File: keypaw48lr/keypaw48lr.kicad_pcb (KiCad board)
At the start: 2 copper layers, 139 x 102 mm, 103 parts, among them J1 Conn_01x02, J2 Conn_01x02, J3 Conn_01x02, J4 Conn_01x02, J5 Conn_01x02, J6 JD9613_OLED_FPC_Conn_01x10, J7 JD9613_OLED_FPC_Conn_01x10, SW1 SW_SPDT, SW2 RotaryEncoder, U1 nice_nano, U2 PAW3395, U3 TLV70019_SOT23-5, U4 TPS22917DBV

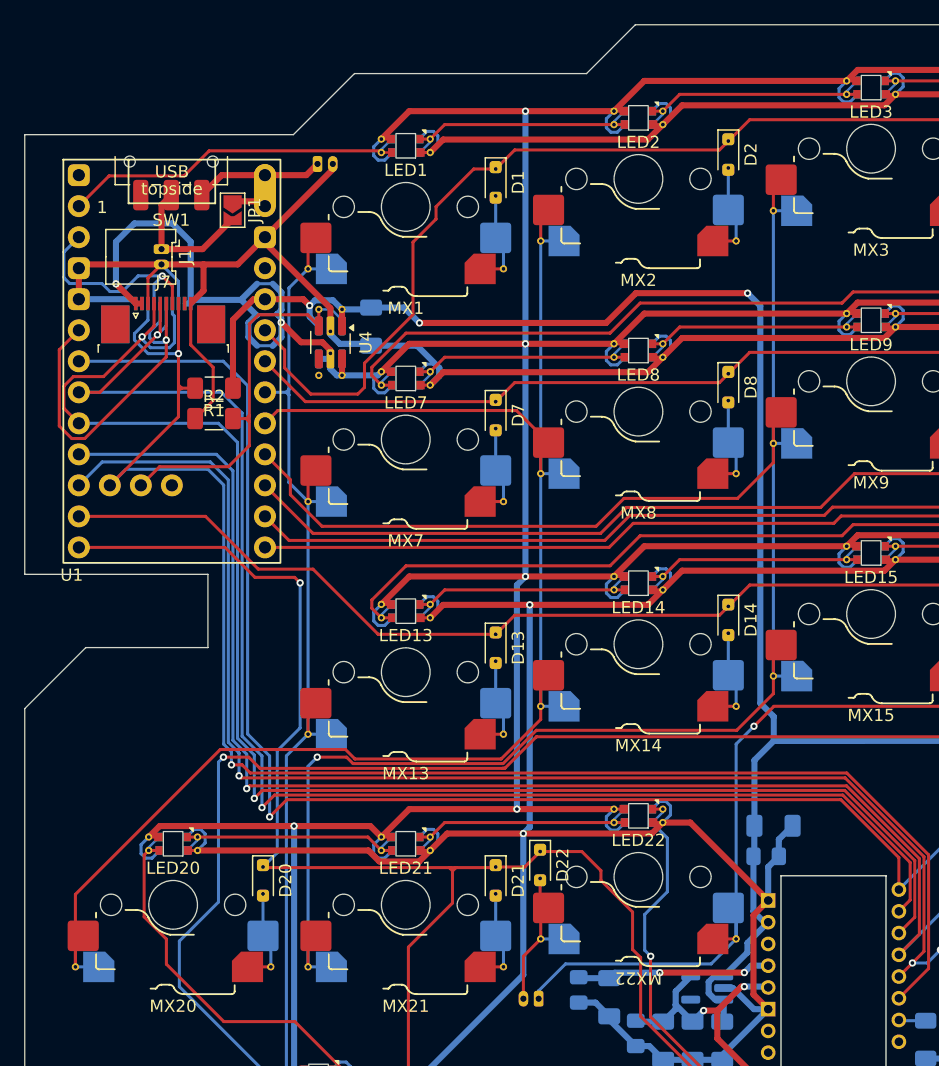
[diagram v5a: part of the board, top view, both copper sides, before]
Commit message: fix: should be able to solder nice!nano on both sides
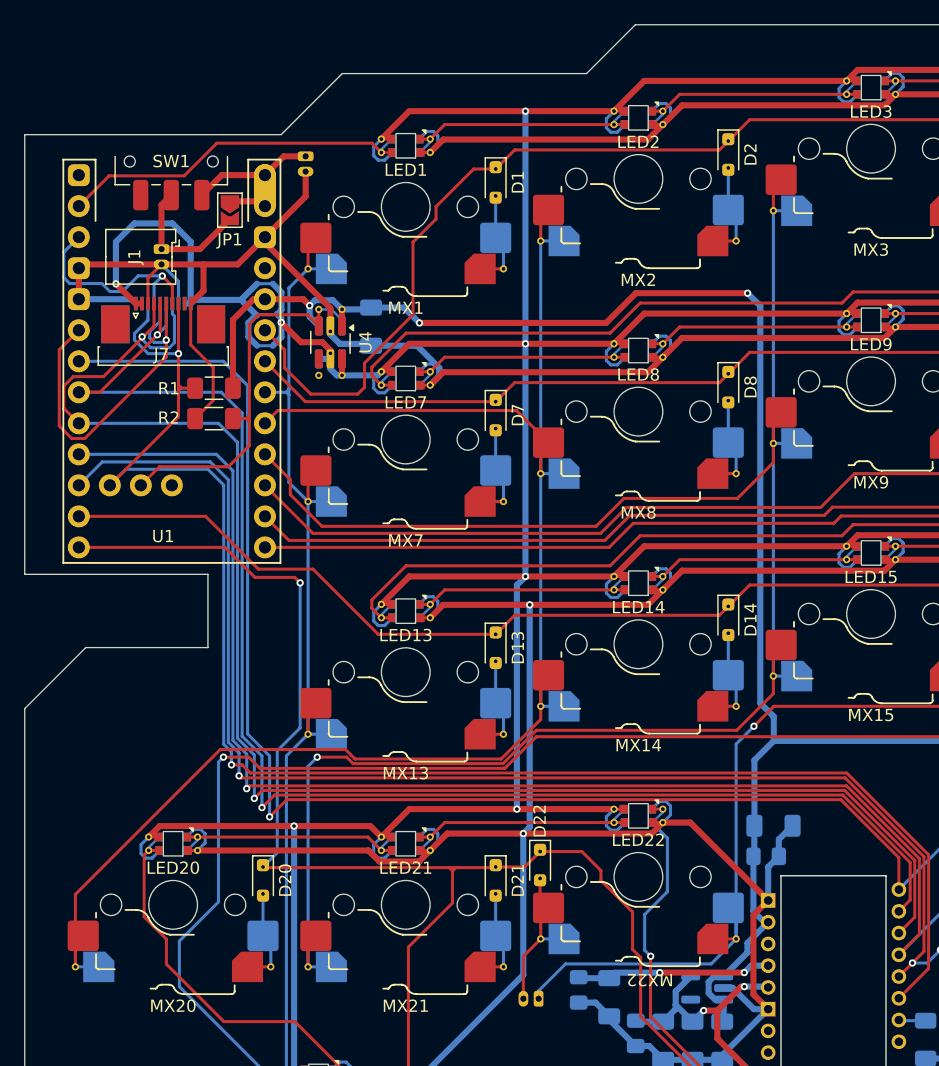
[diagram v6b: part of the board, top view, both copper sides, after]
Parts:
- U1: footprint PCM_marbastlib-xp-promicroish:nice_nano_AH_USBup -> MX_SW_HS_REV:nice_nano_AH_USBup_REV
- moved J2 1.16 mm to (68.0, 57.8), turned to -90 degrees
- moved JP1 0.22 mm to (61.8, 62.2)
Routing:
- net +3.3V: track 191.2 -> 184.0 mm
- net GND: track 761.0 -> 759.5 mm
- net LED: track 29.0 -> 29.5 mm
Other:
- outline, holes or cut-outs redrawn

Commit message: feat: add some more led lights
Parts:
- added LED25: WS2812B, WS2812B_2020_V6:LED_WS2812B-2020_backmount_rev, F.Cu at (56.0, 133.0)
- added LED26: WS2812B, WS2812B_2020_V6:LED_WS2812B-2020_backmount_rev, F.Cu at (85.0, 137.0)
- added LED27: WS2812B, WS2812B_2020_V6:LED_WS2812B-2020_backmount_rev, F.Cu at (119.8, 109.5)
- added LED28: WS2812B, WS2812B_2020_V6:LED_WS2812B-2020_backmount_rev, F.Cu at (132.4, 120.9)
- added LED29: WS2812B, WS2812B_2020_V6:LED_WS2812B-2020_backmount_rev, F.Cu at (152.0, 116.4)
- added LED30: WS2812B, WS2812B_2020_V6:LED_WS2812B-2020_backmount_rev, F.Cu at (171.8, 118.5)
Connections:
- LED19 pad 3: Net-(LED18-DOUT) -> Net-(LED19-DIN)
- LED20 pad 3: Net-(LED19-DOUT) -> Net-(LED20-DIN)
- LED24 pad 1: unconnected-(LED24-DOUT-Pad1) -> Net-(LED24-DOUT)
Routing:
- net GND: track 759.5 -> 896.7 mm
- net V_peri: track 639.4 -> 776.5 mm
- net Net-(LED24-DOUT): track 0.00 -> 76.6 mm
- net Net-(LED20-DIN): track 0.00 -> 52.8 mm
- net Net-(LED29-DOUT): track 0.00 -> 21.8 mm
- net Net-(LED28-DOUT): track 0.00 -> 21.6 mm
- net Net-(LED27-DOUT): track 0.00 -> 20.7 mm
- net Net-(LED19-DOUT): track 32.9 -> 18.6 mm
- net Net-(LED19-DIN): track 0.00 -> 14.2 mm
- net ROW3: track 194.6 -> 200.6 mm
- net Net-(LED18-DOUT): track 164.3 -> 159.5 mm, vias 3 -> 2
- net Net-(D24-A): track 21.7 -> 18.1 mm

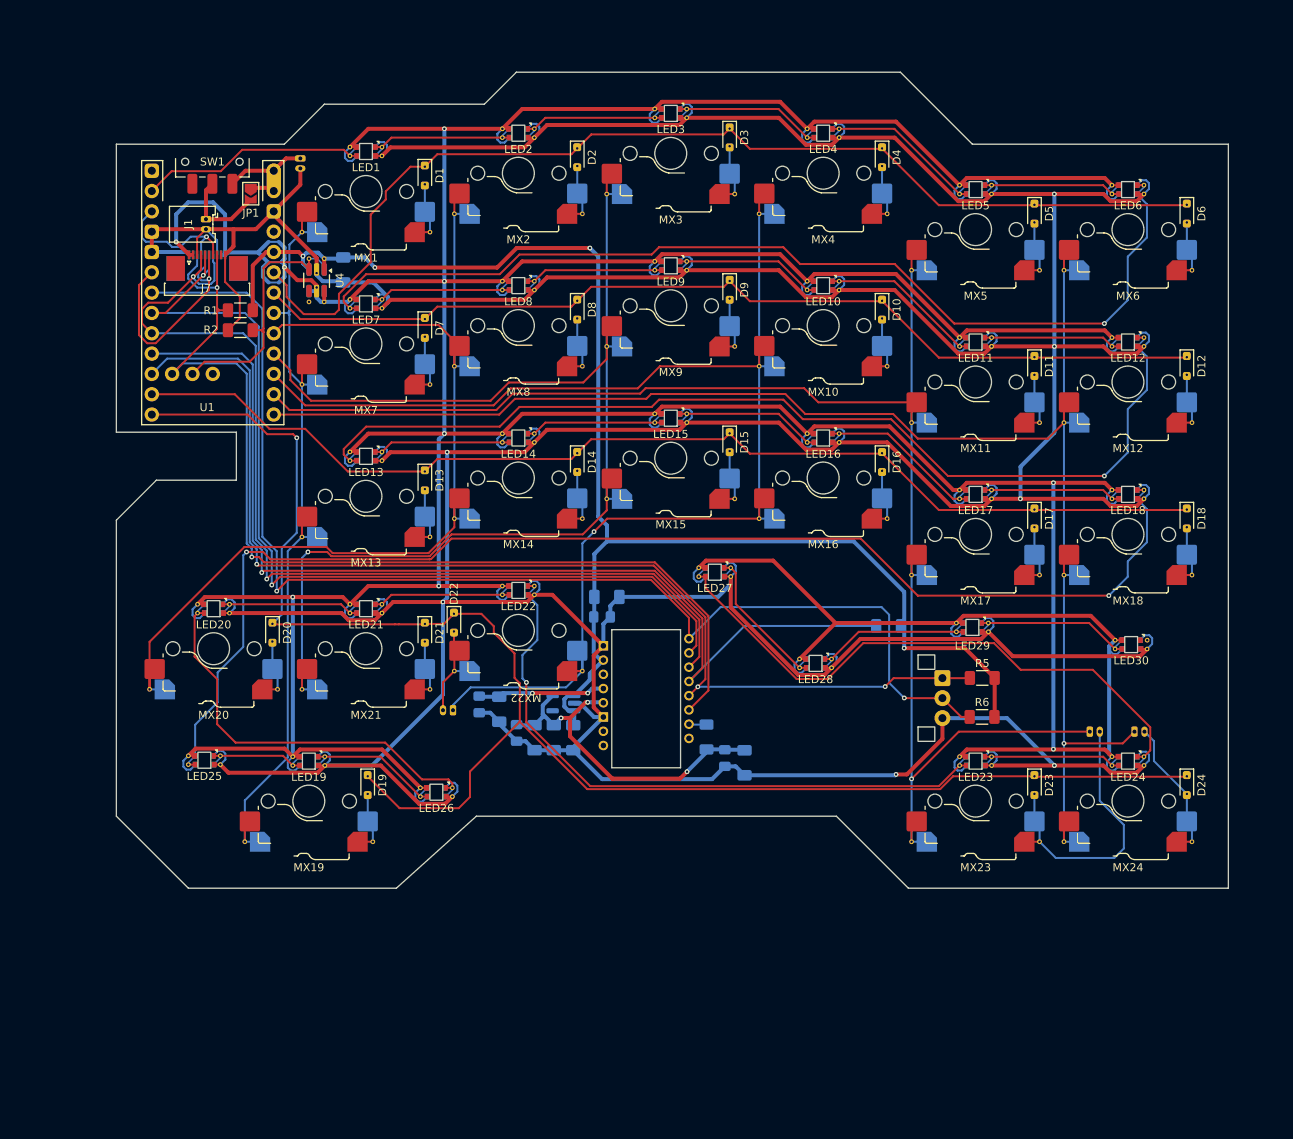
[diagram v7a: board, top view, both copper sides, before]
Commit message: feat: replace encoder with a touch bar
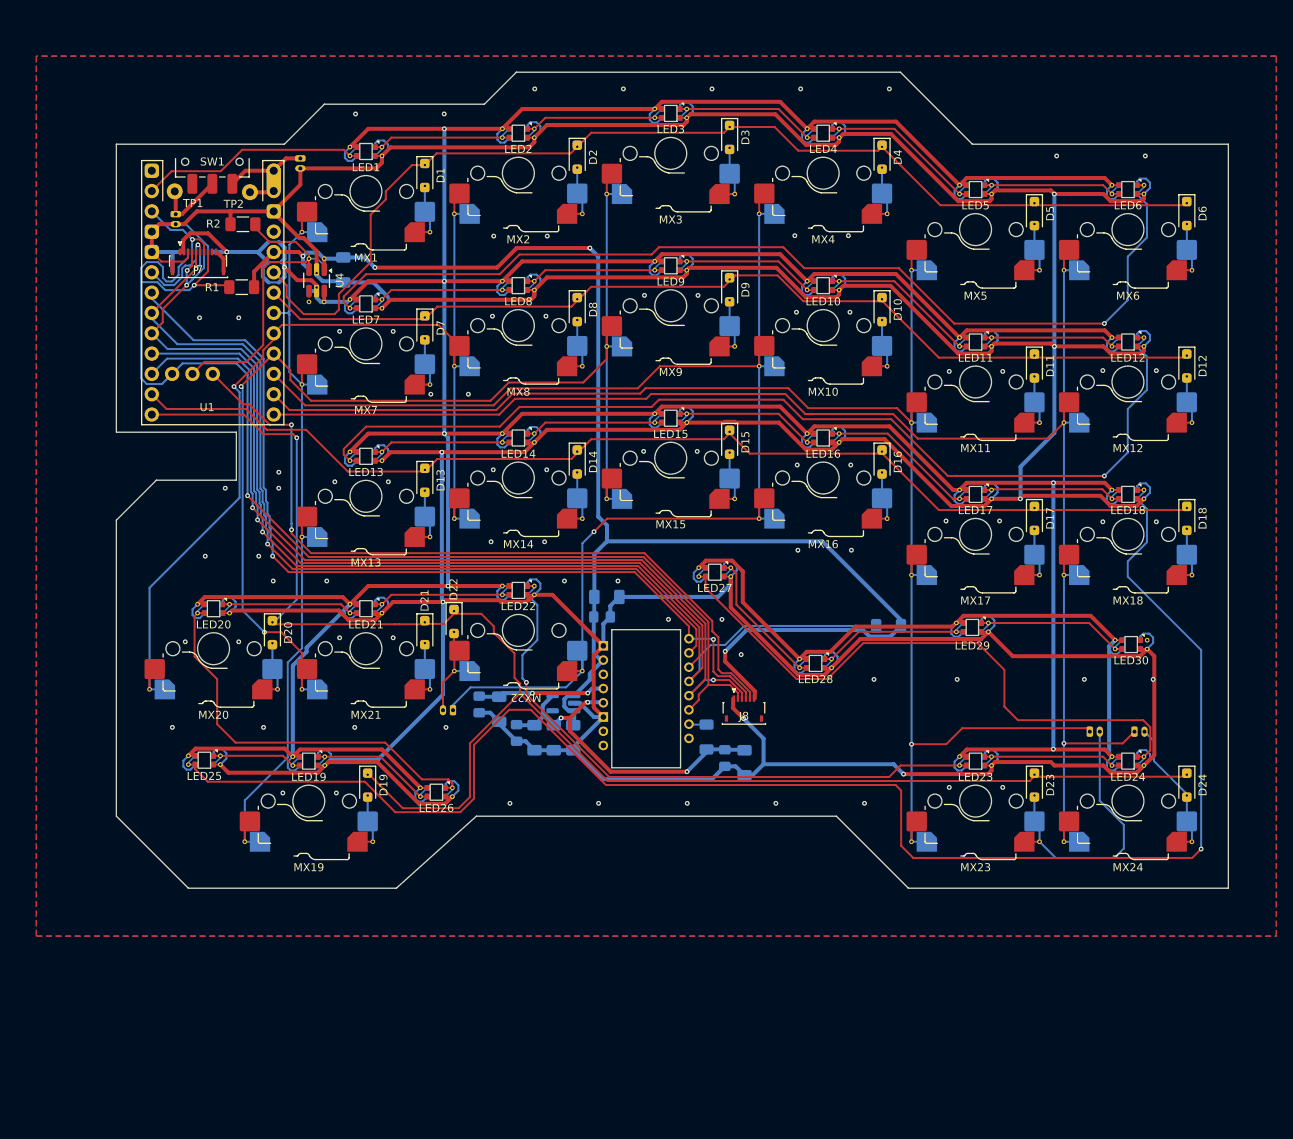
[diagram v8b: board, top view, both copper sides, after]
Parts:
- removed JP1: SolderJumper_2_Open, Jumper:SolderJumper-2_P1.3mm_Open_TrianglePad1.0x1.5mm
- removed R5, R6: 100k, Resistor_SMD:R_1206_3216Metric_Pad1.30x1.75mm_HandSolder
- removed SW2: RotaryEncoder, ALPS_EC10E:RotaryEncoder_Alps_EC10E-Switch
- added J8: DXCL_S2002A_C, DXCL_S2002A_C:FH34SRJ-10S-0.5SH, F.Cu at (123.5, 126.8)
- added TP1: TestPoint, MX_SW_HS_REV:TestPoint_THTPad_D2.0mm_Drill1.0mm_nosilk, F.Cu at (52.3, 61.9)
- added TP2: TestPoint, MX_SW_HS_REV:TestPoint_THTPad_D2.0mm_Drill1.0mm_nosilk, F.Cu at (61.7, 62.0)
- D1, D10, D11, D12, D13, D14, D15, D16, D17, D18, D19, D2, D20, D21, D22, D23, D24, D3, D4, D5, D6, D7, D8, D9: footprint MX_SW_HS_REV:D_SOD-323_HandSoldering_REV -> MX_SW_HS_REV:D_SOD-123_REV
- J1: moved to B.Cu
- J6, J7: footprint JD9613_OLED_FPC:TE_1-1734839-0_1x10-1MP_P0.5mm_Horizontal -> JD9613_OLED_FPC:FH34SRJ-10S-0.5SH
- moved R2 13.2 mm to (60.8, 66.0)
- moved J1 3.83 mm to (52.4, 64.8)
- moved R1 2.89 mm to (60.7, 73.9)
- moved J6 1.15 mm to (55.2, 71.0)
- moved J7 1.15 mm to (55.2, 71.0)
- moved D22 0.14 mm to (87.2, 115.7)
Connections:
- J6 pad MP: unconnected-(J6-PadMP)_1 -> GND
- J7 pad MP: unconnected-(J7-PadMP) -> GND
- U1 pad 27: BUSY -> EINT
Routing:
- net EINT: track 0.00 -> 95.5 mm, vias 0 -> 2
- net GND: track 896.7 -> 942.9 mm, vias 7 -> 85
- net Net-(LED18-DOUT): track 159.5 -> 203.6 mm, vias 2 -> 1
- net MOTION: track 154.8 -> 113.2 mm
- net CS_PAW: track 142.2 -> 112.3 mm, vias 3 -> 2
- net NRESET: track 133.0 -> 152.3 mm
- net CS_OLED: track 29.6 -> 11.1 mm
- net COL2: track 164.3 -> 153.5 mm, vias 1 -> 2
- net SDO: track 128.0 -> 118.3 mm, vias 2 -> 3
- net V_peri: track 776.5 -> 768.2 mm, vias 9 -> 8
- net SCK: track 121.1 -> 113.3 mm
- net DS_OLED: track 18.0 -> 10.8 mm
- net PERI_EN: track 32.4 -> 39.3 mm
- net +3.3V: track 184.0 -> 188.7 mm
- net SDI: track 132.2 -> 128.8 mm
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- added copper zone on B.Cu, net GND
- added copper zone on F.Cu, net GND
